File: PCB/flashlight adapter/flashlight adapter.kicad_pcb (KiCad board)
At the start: 2 copper layers, 30.1 x 30.1 mm, 30 parts, among them J1 USB4105-GF-A, Q1 FS8205A, U1 BQ24074RGT, U2 DW01A, U3 MIC2295YD5-TR

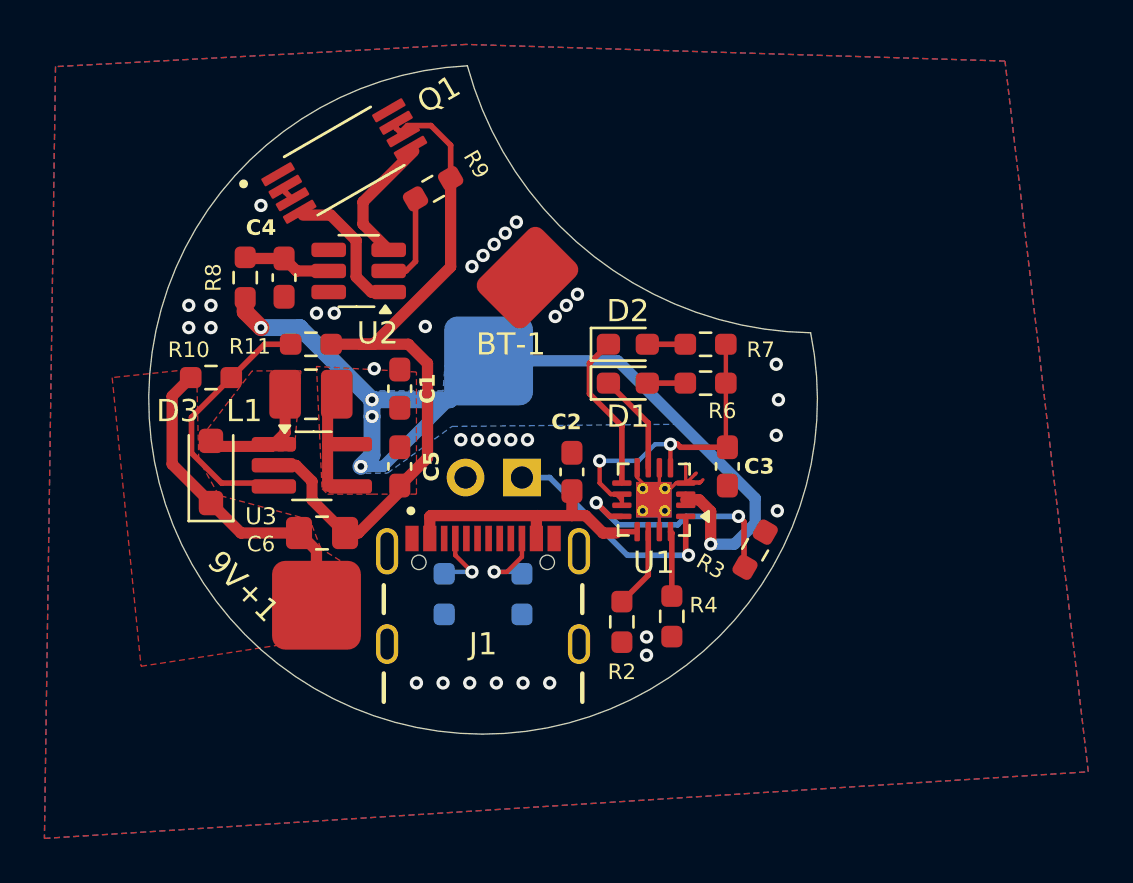
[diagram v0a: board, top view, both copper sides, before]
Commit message: Added Boost off when charging
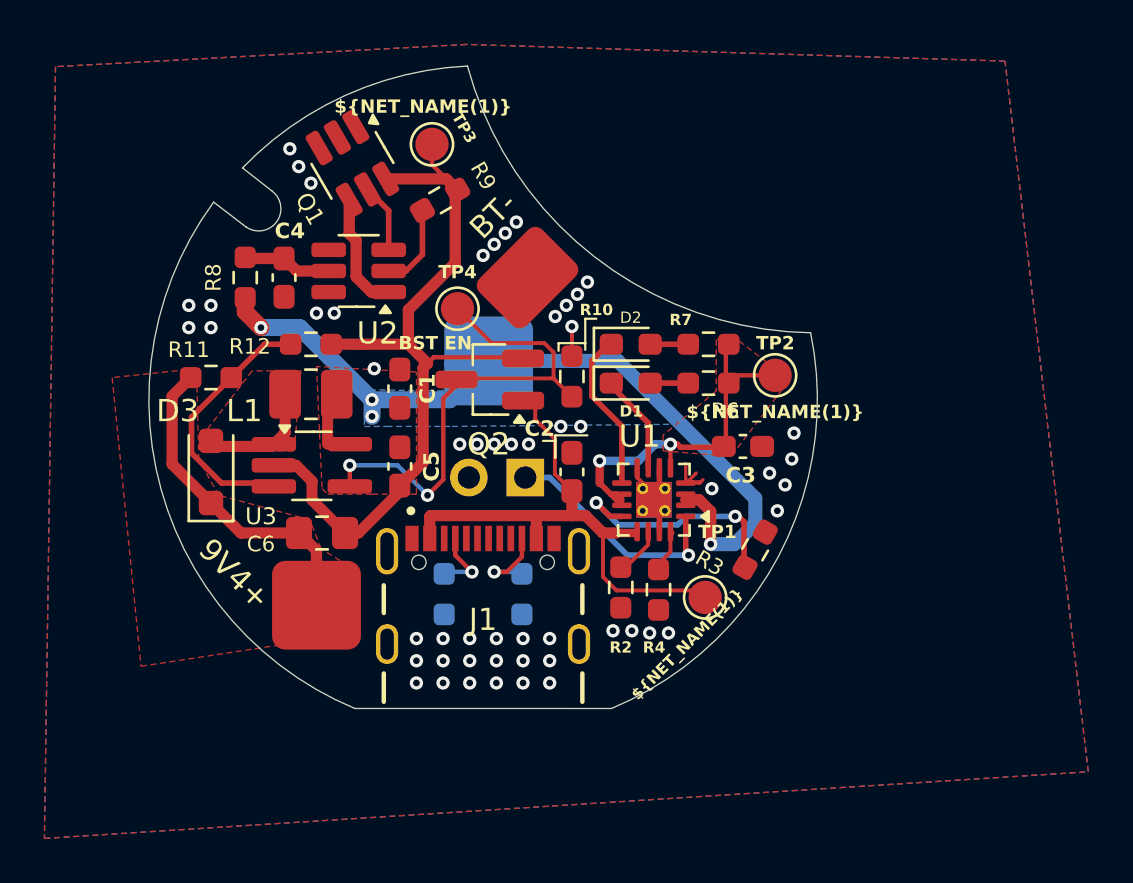
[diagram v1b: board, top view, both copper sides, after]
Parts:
- added G***: LOGO, LOGO, B.Cu at (142.7, 81.7)
- added G***: LOGO, LOGO, B.Cu at (135.6, 93.3)
- added Q2: Q_NMOS_GSD, Package_TO_SOT_SMD:SOT-23_Handsoldering, F.Cu at (145.8, 92.6)
- added R10: 10k, Resistor_SMD:R_0603_1608Metric_Pad0.98x0.95mm_HandSolder, F.Cu at (149.5, 92.5)
- added TP1: VBUS, TestPoint:TestPoint_Pad_D1.5mm, F.Cu at (155.5, 102.4)
- added TP2: OUT, TestPoint:TestPoint_Pad_D1.5mm, F.Cu at (158.7, 92.4)
- added TP3: P+ & BATT+, TestPoint:TestPoint_Pad_D1.5mm, F.Cu at (143.2, 82.0)
- added TP4: BST EN, TestPoint:TestPoint_Pad_D1.5mm, F.Cu at (144.3, 89.4)
- Q1: footprint FS8205A:SOP65P640X120-8N -> Package_TO_SOT_SMD:SOT-23-6_Handsoldering
- moved R2 1.55 mm to (151.7, 102.0)
- moved R4 1.34 mm to (153.4, 102.0)
- moved C3 1.14 mm to (157.2, 95.6), turned to 0 degrees
- moved R9 0.61 mm to (143.6, 84.5)
- moved Q1 0.39 mm to (139.6, 82.9), turned to -60 degrees
- moved TH1 0.15 mm to (147.4, 97.0)
- moved D1 0.13 mm to (152.2, 92.8)
- moved D2 0.13 mm to (152.2, 91.0)
- moved R6 0.13 mm to (155.7, 92.8)
- moved R7 0.13 mm to (155.7, 91.0)
- renumbered 9V+1 to 9V4+, BT-1 to BT-, R10 to R11, R11 to R12
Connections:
- U3 pad 4: /BAT -> Net-(Q2-D)
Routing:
- net Net-(Q2-D): track 0.00 -> 22.8 mm, vias 0 -> 2
- net /VBUS: track 12.8 -> 24.6 mm
- net /BAT: track 49.8 -> 40.7 mm
- net /P-: track 33.5 -> 37.2 mm
- net /EN2: track 14.7 -> 18.2 mm
- net Net-(U2-OC): track 5.87 -> 3.12 mm
- net GND: track 10.3 -> 8.15 mm, vias 34 -> 53
- net Net-(U1-TMR): track 3.64 -> 2.49 mm
- net Net-(U2-OD): track 6.25 -> 5.34 mm
- net Net-(U1-ISET): track 2.93 -> 2.04 mm
- added copper zone on F.Cu, net /EN2
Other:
- board size 30.1 x 30.1 mm -> 30.1 x 28.9 mm
- board text added: "9V li-ion flashlight Adapter V1 Made with <3 by Siwen Long"
